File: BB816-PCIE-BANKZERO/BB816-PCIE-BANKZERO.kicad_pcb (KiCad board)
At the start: 4 copper layers, 167.6 x 111.2 mm, 19 parts, among them J1 BB816_BreakoutA27_PCIex16, J1 SPI_0, J2 LCD Display, J3 LCD Backlight, J4 SPI_1, J5 GPIO, U1 AS7C256B-15PIN, U2 AS7C256B-15PIN, U3 AT28C256-15PU, U4 74HC138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

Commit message: big commit
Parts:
- removed D2, D3: 1N5817, Diode_THT:D_DO-41_SOD81_P10.16mm_Horizontal
- removed J2: LCD Display, Connector_PinSocket_2.54mm:PinSocket_1x16_P2.54mm_Horizontal
- removed J3: LCD Backlight, Connector_PinHeader_2.54mm:PinHeader_1x03_P2.54mm_Horizontal
- removed J4: SPI_1, Connector_PinHeader_2.54mm:PinHeader_1x06_P2.54mm_Horizontal
- removed J5: GPIO, Connector_PinHeader_2.54mm:PinHeader_1x05_P2.54mm_Horizontal
- removed U8: 74HC283, Package_DIP:DIP-16_W7.62mm_Socket
- added R2: 3.3K, Resistor_THT:R_Axial_DIN0207_L6.3mm_D2.5mm_P7.62mm_Horizontal, F.Cu at (189.1, 112.9)
- added R3: 3.3K, Resistor_THT:R_Axial_DIN0207_L6.3mm_D2.5mm_P7.62mm_Horizontal, F.Cu at (194.2, 112.9)
- added R4: 3.3K, Resistor_THT:R_Axial_DIN0207_L6.3mm_D2.5mm_P7.62mm_Horizontal, F.Cu at (199.3, 112.9)
- added U10: 74HC138, Package_DIP:DIP-16_W7.62mm_Socket, F.Cu at (74.8, 105.3)
- added U15: 74HC32, Package_DIP:DIP-14_W7.62mm_Socket, F.Cu at (77.3, 118.0)
- added U16: 74HC138, Package_DIP:DIP-16_W7.62mm_Socket, F.Cu at (176.4, 118.0)
- added U18: 74HC00, Package_DIP:DIP-14_W7.62mm_Socket, F.Cu at (77.3, 130.7)
- added U23: 74HC04, Package_DIP:DIP-14_W7.62mm_Socket, F.Cu at (100.2, 125.6)
- J1: value SPI_0 -> Bypass; footprint Connector_PinHeader_2.54mm:PinHeader_1x06_P2.54mm_Horizontal -> Connector_PinHeader_2.54mm:PinHeader_2x04_P2.54mm_Vertical
- U1, U2: footprint BB816-MATX-PCIE:PDIP-28_MIL300_ALL -> Package_DIP:DIP-28_W7.62mm_Socket
- U5: value 74HC138 -> 74HC148
- U6: value 74HC148 -> 74HC125; footprint Package_DIP:DIP-16_W7.62mm_Socket -> Package_DIP:DIP-14_W7.62mm_Socket
- U7: value 74HC244 -> 74HC283; footprint Package_DIP:DIP-20_W7.62mm_Socket -> Package_DIP:DIP-16_W7.62mm_Socket
- U9: value W65C22SxP -> 74HC32; footprint Package_DIP:DIP-40_W15.24mm_Socket -> Package_DIP:DIP-14_W7.62mm_Socket
- moved U9 126.4 mm to (100.2, 112.9), turned to 90 degrees
- moved U5 98.8 mm to (204.3, 125.6), turned to 90 degrees
- moved U4 90.6 mm to (181.5, 125.6), turned to 90 degrees
- moved U6 83.7 mm to (206.8, 112.9), turned to 90 degrees
- moved J1 68.9 mm to (133.2, 112.9)
- moved RN1 50.7 mm to (222.1, 130.7), turned to 180 degrees
- moved U1 41.7 mm to (120.5, 125.6), turned to 90 degrees
- moved U7 33.8 mm to (158.6, 112.9), turned to 90 degrees
- moved U3 30.8 mm to (120.5, 92.6), turned to 90 degrees
- moved U2 22.6 mm to (120.5, 105.3), turned to 90 degrees
- moved D1 11.0 mm to (182.0, 92.8), turned to -90 degrees
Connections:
- D1 pad 2: Net-(D1-A) -> /~{IRQ}
- J1 pad 1: VCC -> /A4
- J1 pad 2: GND -> /AA4
- J1 pad 3: /PB0 -> /A3
- J1 pad 4: /PB2 -> /AA3
- J1 pad 5: /PB3 -> /A2
- J1 pad 6: /PB4 -> /AA2
- RN1 pad 1: unconnected-(RN1-common-Pad1) -> VCC
- U2 pad 22: /~{RAM1_OE} -> /~{RAM0_OE}
- U2 pad 27: /~{RAM1_WE} -> /~{RAM0_WE}
- U3 pad 11: /D7 -> /D0
- U3 pad 12: /D6 -> /D1
- U3 pad 13: /D5 -> /D2
- U3 pad 15: /D4 -> /D3
- U3 pad 16: /D3 -> /D4
- U3 pad 17: /D2 -> /D5
- U3 pad 18: /D1 -> /D6
- U3 pad 19: /D0 -> /D7
- U3 pad 22: /~{ROM_OE} -> /~{RAM0_OE}
- U3 pad 27: /~{ROM_WE} -> /~{RAM0_WE}
- U4 pad 1: /A1 -> /A2
- U4 pad 12: unconnected-(U4-Y3-Pad12) -> /~{VP_IRQ}
- U4 pad 2: /A2 -> /A3
- U4 pad 3: /A3 -> /A4
- U4 pad 4: /~{VP} -> /E
- U4 pad 6: /E -> /A1
- U4 pad 7: Net-(D2-K) -> unconnected-(U4-Y7-Pad7)
- U5 pad 1: /A2 -> /~{IRQ3}
- U5 pad 10: unconnected-(U5-Y5-Pad10) -> /~{IRQ7}
- U5 pad 11: unconnected-(U5-Y4-Pad11) -> /~{IRQ6}
- U5 pad 12: Net-(D1-K) -> /~{IRQ5}
- U5 pad 13: unconnected-(U5-Y2-Pad13) -> /~{IRQ4}
- U5 pad 14: unconnected-(U5-Y1-Pad14) -> Net-(D1-K)
- U5 pad 2: /A3 -> /~{IRQ2}
- U5 pad 3: /A4 -> /~{IRQ1}
- U5 pad 4: /~{VP} -> /~{IRQ0}
- U5 pad 5: /E -> /~{VP_IRQ}
- U5 pad 6: /A1 -> Net-(U5-S2)
- U5 pad 7: unconnected-(U5-Y7-Pad7) -> Net-(U5-S1)
- U5 pad 9: unconnected-(U5-Y6-Pad9) -> Net-(U5-S0)
- U6 pad 1: /~{IRQ3} -> Net-(D1-K)
- U6 pad 10: /~{IRQ7} -> VCC
- U6 pad 11: /~{IRQ6} -> /OFF3
- U6 pad 12: /~{IRQ5} -> Net-(U5-S2)
- U6 pad 13: /~{IRQ4} -> Net-(D1-K)
- U6 pad 14: Net-(D3-K) -> VCC
- U6 pad 2: /~{IRQ2} -> Net-(U5-S1)
- U6 pad 3: /~{IRQ1} -> /OFF2
- U6 pad 4: /~{IRQ0} -> Net-(D1-K)
- U6 pad 5: Net-(D1-A) -> Net-(U5-S0)
- U6 pad 6: Net-(U6-S2) -> /OFF1
- U6 pad 7: Net-(U6-S1) -> GND
- U6 pad 8: GND -> unconnected-(U6-Pad8)
- U6 pad 9: Net-(U6-S0) -> GND
- U7 pad 1: VCC -> /AA2
- U7 pad 10: GND -> /AA4
- U7 pad 11: Net-(U6-S2) -> GND
- U7 pad 12: unconnected-(U7-1Y3-Pad12) -> /A4
- U7 pad 13: Net-(U6-S1) -> /AA3
- U7 pad 14: unconnected-(U7-1Y2-Pad14) -> /A3
- U7 pad 15: Net-(U6-S0) -> /OFF3
- U7 pad 16: unconnected-(U7-1Y1-Pad16) -> VCC
- U7 pad 2: VCC -> /OFF2
- U7 pad 3: unconnected-(U7-2Y0-Pad3) -> /A2
- U7 pad 4: VCC -> /AA1
- U7 pad 5: Net-(U7-2Y1) -> /A1
- U7 pad 6: VCC -> /OFF1
- U7 pad 7: Net-(U7-2Y2) -> GND
- U7 pad 8: VCC -> GND
- U7 pad 9: Net-(U7-2Y3) -> unconnected-(U7-C4-Pad9)
- U9 pad 1: GND -> /~{BANK0}
- U9 pad 10: /PB0 -> /A8
- U9 pad 11: /PB1 -> /~{32K_HI}
- U9 pad 12: /PB2 -> /~{BANK0}
- U9 pad 13: /PB3 -> /~{A15}
- U9 pad 14: /PB4 -> VCC
- U9 pad 2: /PA0 -> /A15
- U9 pad 3: /PA1 -> /~{RAM0_CE}
- U9 pad 4: /PA2 -> Net-(U10-Y7)
- U9 pad 5: /PA3 -> Net-(U9-Pad5)
- U9 pad 6: /PA4 -> /~{IO_PAGE}
- U9 pad 7: /PA5 -> GND
- U9 pad 8: /PA6 -> Net-(U9-Pad5)
- U9 pad 9: /PA7 -> /~{A9}
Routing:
- net /A1: track 0.00 -> 74.8 mm
- net /E: track 0.00 -> 74.7 mm, vias 0 -> 1
- net /~{VP}: track 0.00 -> 74.2 mm, vias 0 -> 1
- net /~{IO_PAGE}: track 0.00 -> 73.8 mm
- net /~{IRQ7}: track 0.00 -> 64.4 mm
- net /~{IRQ6}: track 0.00 -> 60.9 mm
- net /~{IRQ5}: track 0.00 -> 57.3 mm
- net /~{IRQ0}: track 0.00 -> 57.1 mm
- net /~{IRQ1}: track 0.00 -> 54.8 mm
- net /~{IRQ4}: track 0.00 -> 53.8 mm
- net /~{IRQ2}: track 0.00 -> 53.5 mm
- net /~{IRQ3}: track 0.00 -> 51.6 mm
- net /A5: track 0.00 -> 49.8 mm, vias 0 -> 1
- net /A6: track 0.00 -> 48.0 mm, vias 0 -> 1
- net /A7: track 0.00 -> 46.3 mm, vias 0 -> 1
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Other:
- board text removed: "WARNING: Not for use with PCIe Bus"

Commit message: Bum AND
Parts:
- removed U18: 74HC00, Package_DIP:DIP-14_W7.62mm_Socket
- J1: value BB816_BreakoutA27_PCIex16 -> Bypass; footprint BB816-MATX-PCIE:PCIexpress_x16_HW_FH -> Connector_PinHeader_2.54mm:PinHeader_2x04_P2.54mm_Vertical
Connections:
- U23 pad 1: /~{RAM0_OE} -> (no net)
- U23 pad 2: /RD -> (no net)
- U6 pad 10: VCC -> /~{RAM0_OE}
- U6 pad 8: unconnected-(U6-Pad8) -> /EMU_RD
- U6 pad 9: GND -> /E
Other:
- board outline removed

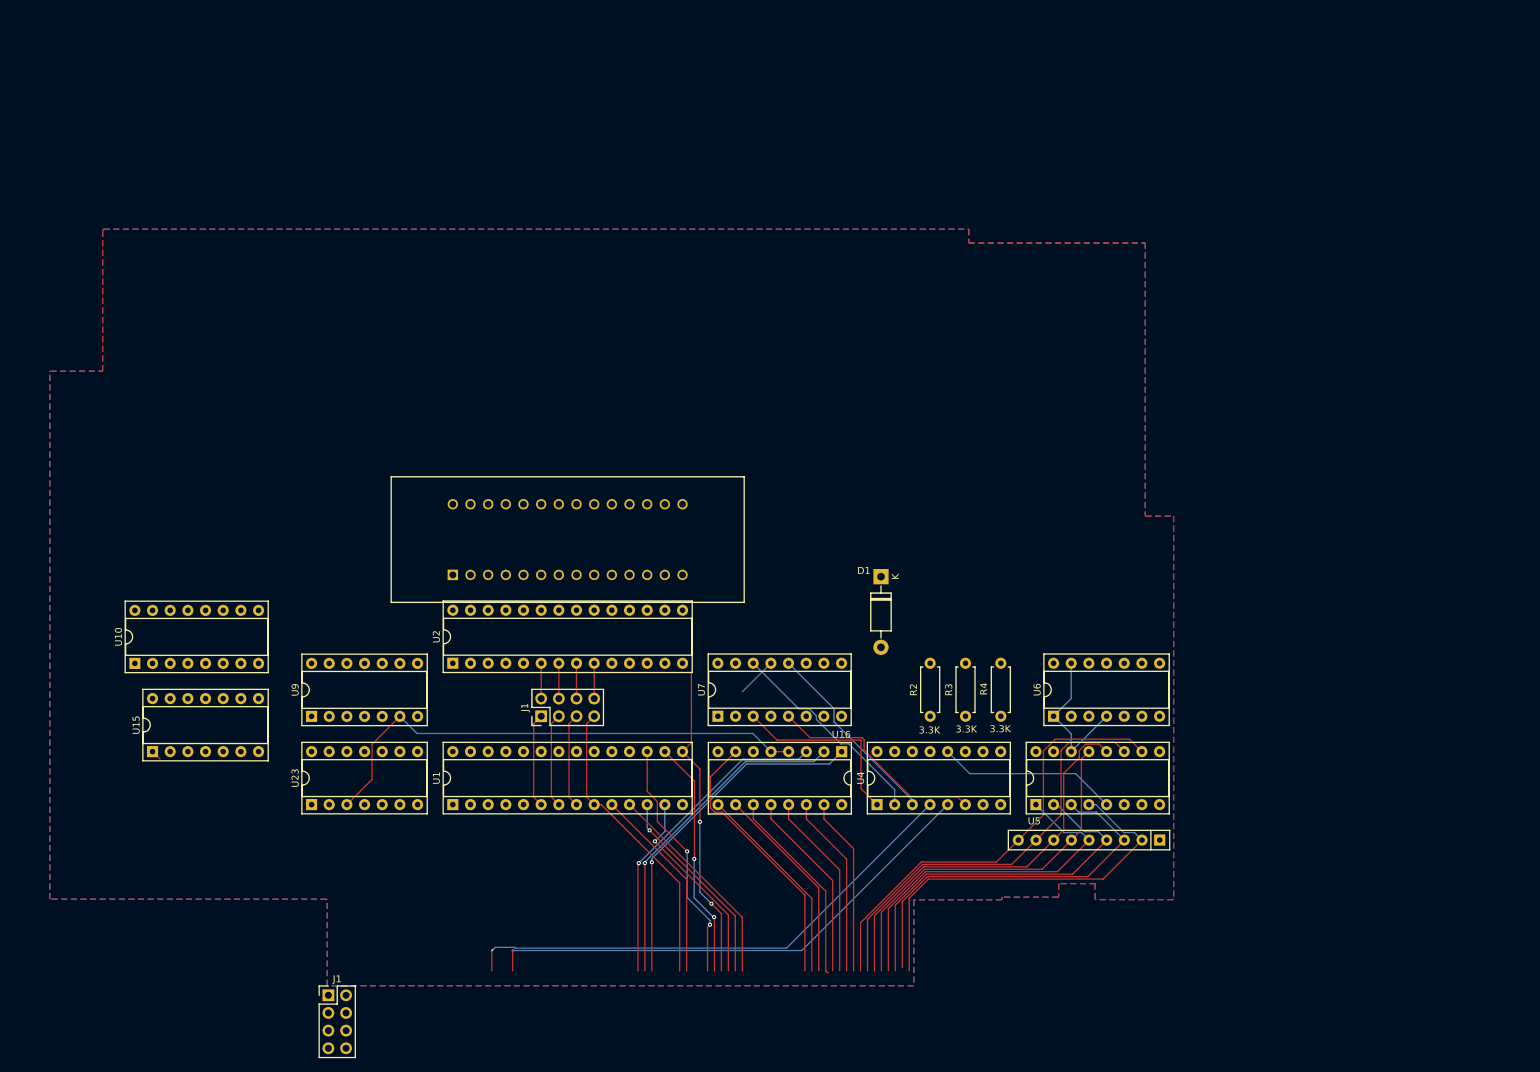
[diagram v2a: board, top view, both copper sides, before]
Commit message: Add VIA and ACIA
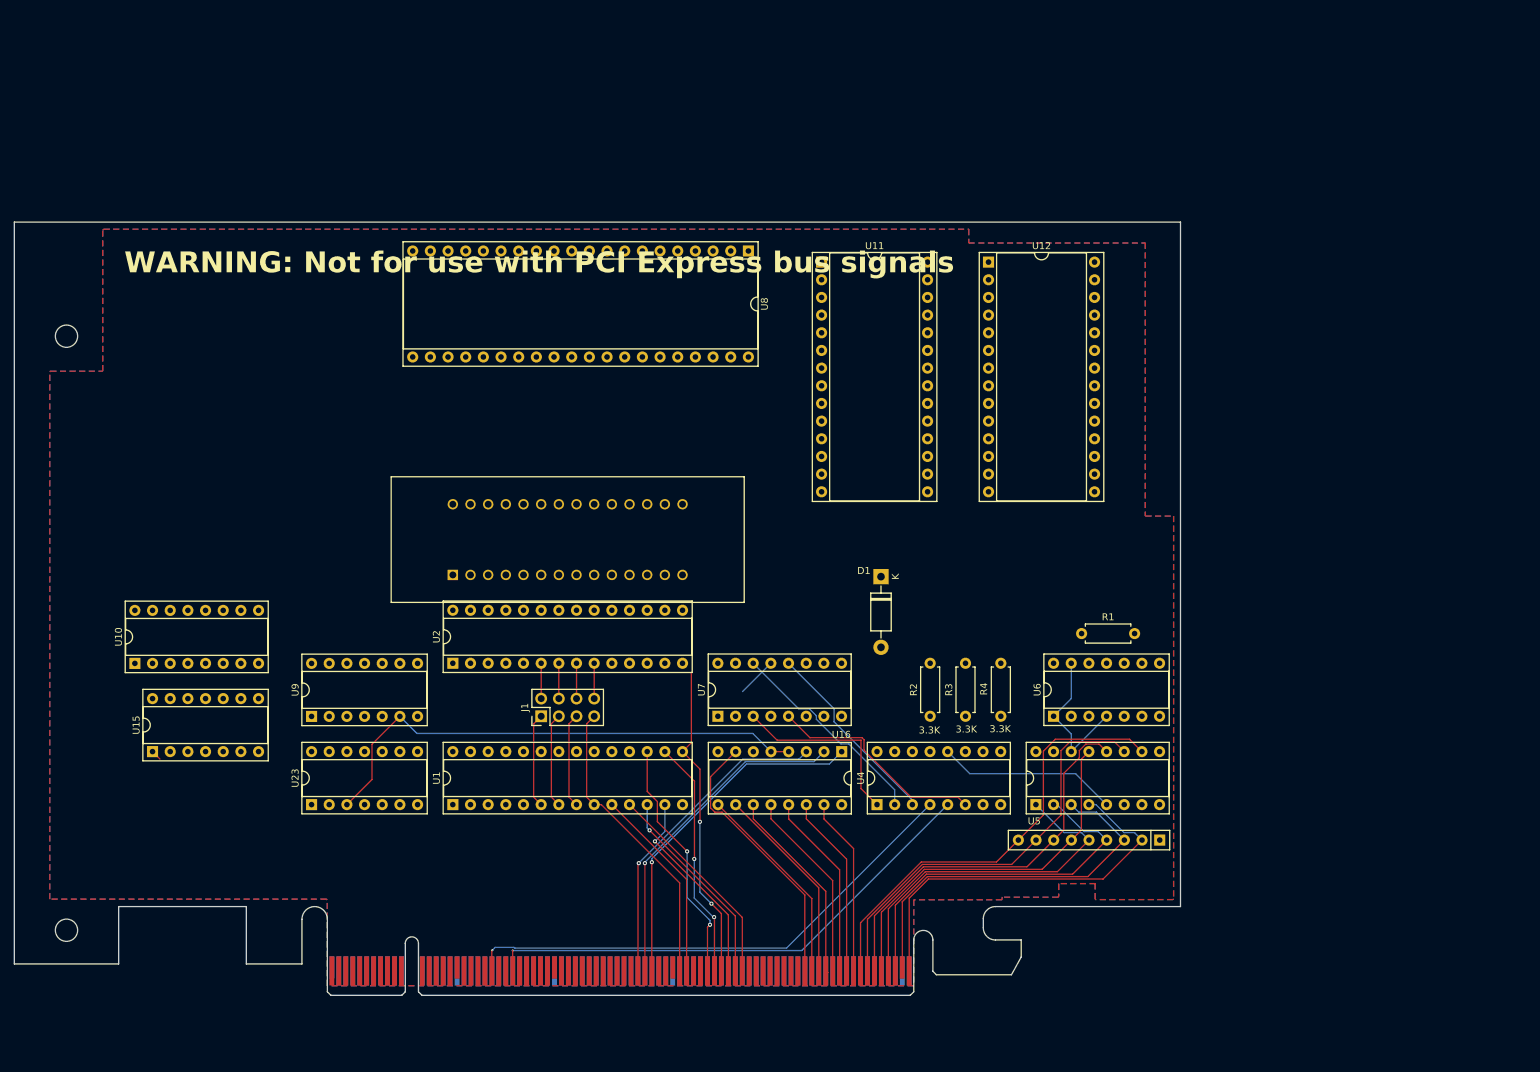
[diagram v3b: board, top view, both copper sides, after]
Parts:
- added R1: 3.3K, Resistor_THT:R_Axial_DIN0207_L6.3mm_D2.5mm_P7.62mm_Horizontal, F.Cu at (210.9, 101.0)
- added U11: W65C51NxP, Package_DIP:DIP-28_W15.24mm_Socket, F.Cu at (173.5, 47.6)
- added U12: W65C51NxP, Package_DIP:DIP-28_W15.24mm_Socket, F.Cu at (197.5, 47.6)
- added U8: W65C22SxP, Package_DIP:DIP-40_W15.24mm_Socket, F.Cu at (163.0, 46.0)
- J1: value Bypass -> BB816_BreakoutA27_PCIex16; footprint Connector_PinHeader_2.54mm:PinHeader_2x04_P2.54mm_Vertical -> BB816-MATX-PCIE:PCIexpress_x16_HW_FH
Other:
- board outline added: 167.6 x 111.2 mm
- board text added: "WARNING: Not for use with PCI Express bus signals"

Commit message: VIA
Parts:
- removed U11: W65C51NxP, Package_DIP:DIP-28_W15.24mm_Socket
- added J2: Conn_01x22_Pin, Connector_PinHeader_2.54mm:PinHeader_1x22_P2.54mm_Horizontal, B.Cu at (186.5, 24.0)
- moved U12 61.6 mm to (258.1, 36.9)
- moved J1 31.0 mm to (110.9, 123.1)
- moved U8 23.2 mm to (178.9, 29.1)
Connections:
- U8 pad 1: unconnected-(U8-VSS-Pad1) -> GND
- U8 pad 10: unconnected-(U8-PB0-Pad10) -> Net-(J2-Pin_13)
- U8 pad 11: unconnected-(U8-PB1-Pad11) -> Net-(J2-Pin_14)
- U8 pad 12: unconnected-(U8-PB2-Pad12) -> Net-(J2-Pin_15)
- U8 pad 13: unconnected-(U8-PB3-Pad13) -> Net-(J2-Pin_16)
- U8 pad 14: unconnected-(U8-PB4-Pad14) -> Net-(J2-Pin_17)
- U8 pad 15: unconnected-(U8-PB5-Pad15) -> Net-(J2-Pin_18)
- U8 pad 16: unconnected-(U8-PB6-Pad16) -> Net-(J2-Pin_19)
- U8 pad 17: unconnected-(U8-PB7-Pad17) -> Net-(J2-Pin_20)
- U8 pad 18: unconnected-(U8-CB1-Pad18) -> Net-(J2-Pin_21)
- U8 pad 19: unconnected-(U8-CB2-Pad19) -> Net-(J2-Pin_22)
- U8 pad 2: unconnected-(U8-PA0-Pad2) -> Net-(J2-Pin_3)
- U8 pad 20: unconnected-(U8-VCC-Pad20) -> VCC
- U8 pad 21: unconnected-(U8-~{IRQ}-Pad21) -> /~{IRQ0}
- U8 pad 22: unconnected-(U8-R/~{W}-Pad22) -> /~{RAM0_WE}
- U8 pad 23: unconnected-(U8-~{CS2}-Pad23) -> /~{IOCS0}
- U8 pad 24: unconnected-(U8-CS1-Pad24) -> VCC
- U8 pad 26: unconnected-(U8-D7-Pad26) -> /D7
- U8 pad 27: unconnected-(U8-D6-Pad27) -> /D6
- U8 pad 28: unconnected-(U8-D5-Pad28) -> /D5
- U8 pad 29: unconnected-(U8-D4-Pad29) -> /D4
- U8 pad 3: unconnected-(U8-PA1-Pad3) -> Net-(J2-Pin_4)
- U8 pad 30: unconnected-(U8-D3-Pad30) -> /D3
- U8 pad 31: unconnected-(U8-D2-Pad31) -> /D2
- U8 pad 32: unconnected-(U8-D1-Pad32) -> /D1
- U8 pad 33: unconnected-(U8-D0-Pad33) -> /D0
- U8 pad 35: unconnected-(U8-RS3-Pad35) -> /A3
- U8 pad 36: unconnected-(U8-RS2-Pad36) -> /A2
- U8 pad 37: unconnected-(U8-RS1-Pad37) -> /A1
- U8 pad 38: unconnected-(U8-RS0-Pad38) -> /A0
- U8 pad 39: unconnected-(U8-CA2-Pad39) -> Net-(J2-Pin_12)
- U8 pad 4: unconnected-(U8-PA2-Pad4) -> Net-(J2-Pin_5)
- U8 pad 40: unconnected-(U8-CA1-Pad40) -> Net-(J2-Pin_11)
- U8 pad 5: unconnected-(U8-PA3-Pad5) -> Net-(J2-Pin_6)
- U8 pad 6: unconnected-(U8-PA4-Pad6) -> Net-(J2-Pin_7)
- U8 pad 7: unconnected-(U8-PA5-Pad7) -> Net-(J2-Pin_8)
- U8 pad 8: unconnected-(U8-PA6-Pad8) -> Net-(J2-Pin_9)
- U8 pad 9: unconnected-(U8-PA7-Pad9) -> Net-(J2-Pin_10)
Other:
- board size 167.6 x 111.2 mm -> 167.6 x 111.1 mm
- board text removed: "WARNING: Not for use with PCI Express bus signals"

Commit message: Stuff
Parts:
- removed the J1 at (110.9, 123.1)
- added REF**: BUS_PCIexpress_x16, BB816-MATX-PCIE:PCIexpress_x16_HW_FH, F.Cu at (57.5, 42.2)
- J2: footprint Connector_PinHeader_2.54mm:PinHeader_1x22_P2.54mm_Horizontal -> Connector_PinSocket_2.54mm:PinSocket_1x22_P2.54mm_Horizontal; moved to F.Cu
- moved U12 62.9 mm to (197.0, 51.6)
- moved U8 29.4 mm to (178.9, 58.4)
- moved J2 29.1 mm to (186.5, 53.0), turned to -90 degrees
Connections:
- net Net-(J2-Pin_13) renamed /PB0
- net Net-(J2-Pin_14) renamed /PB1
- net Net-(J2-Pin_15) renamed /PB2
- net Net-(J2-Pin_16) renamed /PB3
- net Net-(J2-Pin_17) renamed /PB4
- net Net-(J2-Pin_18) renamed /PB5
- net Net-(J2-Pin_19) renamed /PB6
- net Net-(J2-Pin_20) renamed /PB7
- net Net-(J2-Pin_21) renamed /CB1
- net Net-(J2-Pin_22) renamed /CB2
- J2 pad 1: unconnected-(J2-Pin_1-Pad1) -> VCC
- J2 pad 10: Net-(J2-Pin_10) -> /PA5
- J2 pad 11: Net-(J2-Pin_11) -> /PA6
- J2 pad 12: Net-(J2-Pin_12) -> /PA7
- J2 pad 2: unconnected-(J2-Pin_2-Pad2) -> GND
- J2 pad 3: Net-(J2-Pin_3) -> /CA1
- J2 pad 4: Net-(J2-Pin_4) -> /CA2
- J2 pad 5: Net-(J2-Pin_5) -> /PA0
- J2 pad 6: Net-(J2-Pin_6) -> /PA1
- J2 pad 7: Net-(J2-Pin_7) -> /PA2
- J2 pad 8: Net-(J2-Pin_8) -> /PA3
- J2 pad 9: Net-(J2-Pin_9) -> /PA4
- U8 pad 2: Net-(J2-Pin_3) -> /PA0
- U8 pad 25: unconnected-(U8-ϕ2-Pad25) -> /CLK
- U8 pad 3: Net-(J2-Pin_4) -> /PA1
- U8 pad 39: Net-(J2-Pin_12) -> /CA2
- U8 pad 4: Net-(J2-Pin_5) -> /PA2
- U8 pad 40: Net-(J2-Pin_11) -> /CA1
- U8 pad 5: Net-(J2-Pin_6) -> /PA3
- U8 pad 6: Net-(J2-Pin_7) -> /PA4
- U8 pad 7: Net-(J2-Pin_8) -> /PA5
- U8 pad 8: Net-(J2-Pin_9) -> /PA6
- U8 pad 9: Net-(J2-Pin_10) -> /PA7
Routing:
- net /PB7: track 0.00 -> 5.37 mm
- net /PB6: track 0.00 -> 5.37 mm
- net /PB5: track 0.00 -> 5.37 mm
- net /CB2: track 0.00 -> 5.37 mm
- net /CB1: track 0.00 -> 5.37 mm
- added copper zone on B.Cu, net (none)
- added copper zone on F.Cu, net (none)
- added copper zone on In1.Cu, net (none)
- added copper zone on In2.Cu, net (none)
- removed copper zone on In1.Cu, net GND
- removed copper zone on In2.Cu, net GND
- removed copper zone on B.Cu, net VCC
- removed copper zone on F.Cu, net VCC
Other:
- board size 167.6 x 111.1 mm -> 167.7 x 111.1 mm
